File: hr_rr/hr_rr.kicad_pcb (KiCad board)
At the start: 2 copper layers, 5 parts, among them J1 Conn_01x02_Male, U1 TPS62746, U2 TPS63051_YFF, U3 nRF52840, U4 ADAS1000-4BCPZ

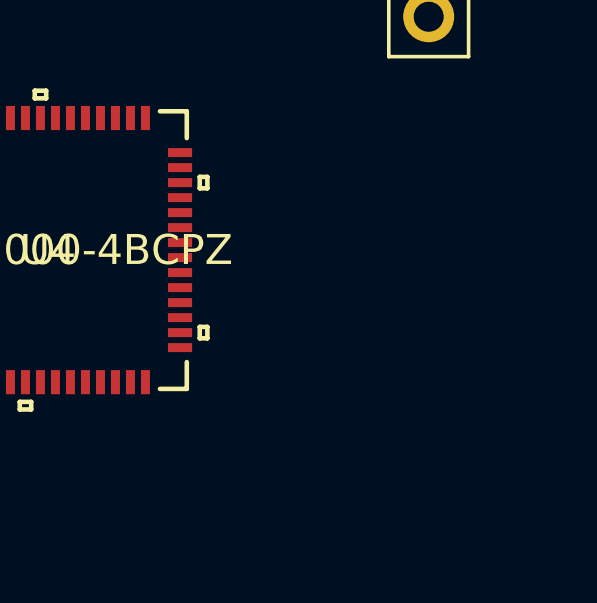
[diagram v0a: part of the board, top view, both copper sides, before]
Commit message: Restored original nRF52832 design.
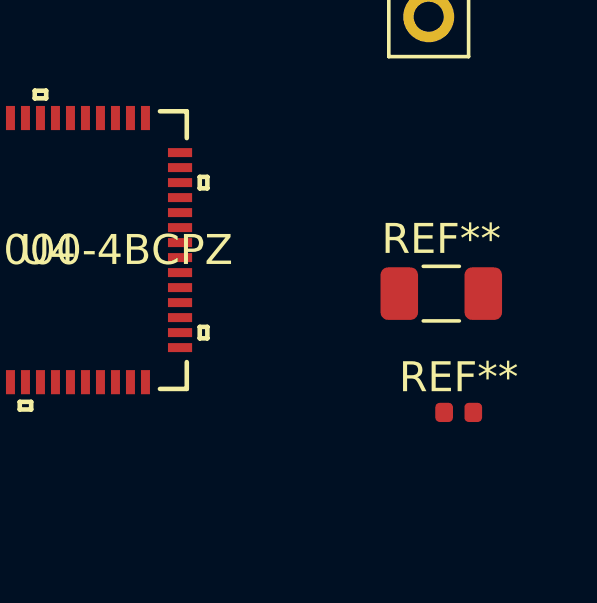
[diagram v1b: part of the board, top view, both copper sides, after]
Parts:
- added REF**: R_0402_1005Metric, Resistor_SMD:R_0402_1005Metric, F.Cu at (108.0, 72.3)
- added REF**: R_1206_3216Metric, Resistor_SMD:R_1206_3216Metric, F.Cu at (107.5, 68.4)
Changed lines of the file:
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@@
     (tracks 0)
     (zones 0)
-    (modules 5)
+    (modules 7)
     (nets 148)
   )
@@
     (pad_to_mask_clearance 0.2)
     (aux_axis_origin 0 0)
-    (visible_elements FFFFFF7F)
+    (visible_elements 7FFFFFFF)
     (pcbplotparams
       (layerselection 0x010fc_ffffffff)
@@
       (net 147 "Net-(U4-Pad56)"))
   )
+  (module Resistor_SMD:R_0402_1005Metric (layer F.Cu)
+    (at 108.04 72.34)
+    (descr "Resistor SMD 0402 (1005 Metric), square (rectangular) end terminal, IPC_7351 nominal, (Body size source: http://www.tortai-tech.com/upload/download/2011102023233369053.pdf), generated with kicad-footprint-generator")
+    (tags resistor)
+    (attr smd)
+    (fp_text reference REF** (at 0 -1.17) (layer F.SilkS)
+      (effects (font (size 1 1) (thickness 0.15)))
+    )
+    (fp_text value R_0402_1005Metric (at 0 1.17) (layer F.Fab)
+      (effects (font (size 1 1) (thickness 0.15)))
+    )
+    (fp_text user %R (at 0 0) (layer F.Fab)
+      (effects (font (size 0.25 0.25) (thickness 0.04)))
+    )
+    (fp_line (start 0.93 0.47) (end -0.93 0.47) (layer F.CrtYd) (width 0.05))
+    (fp_line (start 0.93 -0.47) (end 0.93 0.47) (layer F.CrtYd) (width 0.05))
+    (fp_line (start -0.93 -0.47) (end 0.93 -0.47) (layer F.CrtYd) (width 0.05))
+    (fp_line (start -0.93 0.47) (end -0.93 -0.47) (layer F.CrtYd) (width 0.05))
+    (fp_line (start 0.5 0.25) (end -0.5 0.25) (layer F.Fab) (width 0.1))
+    (fp_line (start 0.5 -0.25) (end 0.5 0.25) (layer F.Fab) (width 0.1))
+    (fp_line (start -0.5 -0.25) (end 0.5 -0.25) (layer F.Fab) (width 0.1))
+    (fp_line (start -0.5 0.25) (end -0.5 -0.25) (layer F.Fab) (width 0.1))
+    (pad 2 smd roundrect (at 0.485 0) (size 0.59 0.64) (layers F.Cu F.Paste F.Mask) (roundrect_rratio 0.25))
+    (pad 1 smd roundrect (at -0.485 0) (size 0.59 0.64) (layers F.Cu F.Paste F.Mask) (roundrect_rratio 0.25))
+    (model ${KISYS3DMOD}/Resistor_SMD.3dshapes/R_0402_1005Metric.wrl
+      (at (xyz 0 0 0))
+      (scale (xyz 1 1 1))
+      (rotate (xyz 0 0 0))
+    )
+  )
+  (module Resistor_SMD:R_1206_3216Metric (layer F.Cu)
+    (at 107.46 68.38)
+    (descr "Resistor SMD 1206 (3216 Metric), square (rectangular) end terminal, IPC_7351 nominal, (Body size source: http://www.tortai-tech.com/upload/download/2011102023233369053.pdf), generated with kicad-footprint-generator")
+    (tags resistor)
+    (attr smd)
+    (fp_text reference REF** (at 0 -1.82) (layer F.SilkS)
+      (effects (font (size 1 1) (thickness 0.15)))
+    )
+    (fp_text value R_1206_3216Metric (at 0 1.82) (layer F.Fab)
+      (effects (font (size 1 1) (thickness 0.15)))
+    )
+    (fp_text user %R (at 0 0) (layer F.Fab)
+      (effects (font (size 0.8 0.8) (thickness 0.12)))
+    )
+    (fp_line (start 2.28 1.12) (end -2.28 1.12) (layer F.CrtYd) (width 0.05))
+    (fp_line (start 2.28 -1.12) (end 2.28 1.12) (layer F.CrtYd) (width 0.05))
+    (fp_line (start -2.28 -1.12) (end 2.28 -1.12) (layer F.CrtYd) (width 0.05))
+    (fp_line (start -2.28 1.12) (end -2.28 -1.12) (layer F.CrtYd) (width 0.05))
+    (fp_line (start -0.602064 0.91) (end 0.602064 0.91) (layer F.SilkS) (width 0.12))
+    (fp_line (start -0.602064 -0.91) (end 0.602064 -0.91) (layer F.SilkS) (width 0.12))
+    (fp_line (start 1.6 0.8) (end -1.6 0.8) (layer F.Fab) (width 0.1))
+    (fp_line (start 1.6 -0.8) (end 1.6 0.8) (layer F.Fab) (width 0.1))
+    (fp_line (start -1.6 -0.8) (end 1.6 -0.8) (layer F.Fab) (width 0.1))
+    (fp_line (start -1.6 0.8) (end -1.6 -0.8) (layer F.Fab) (width 0.1))
+    (pad 2 smd roundrect (at 1.4 0) (size 1.25 1.75) (layers F.Cu F.Paste F.Mask) (roundrect_rratio 0.2))
+    (pad 1 smd roundrect (at -1.4 0) (size 1.25 1.75) (layers F.Cu F.Paste F.Mask) (roundrect_rratio 0.2))
+    (model ${KISYS3DMOD}/Resistor_SMD.3dshapes/R_1206_3216Metric.wrl
+      (at (xyz 0 0 0))
+      (scale (xyz 1 1 1))
+      (rotate (xyz 0 0 0))
+    )
+  )
 )

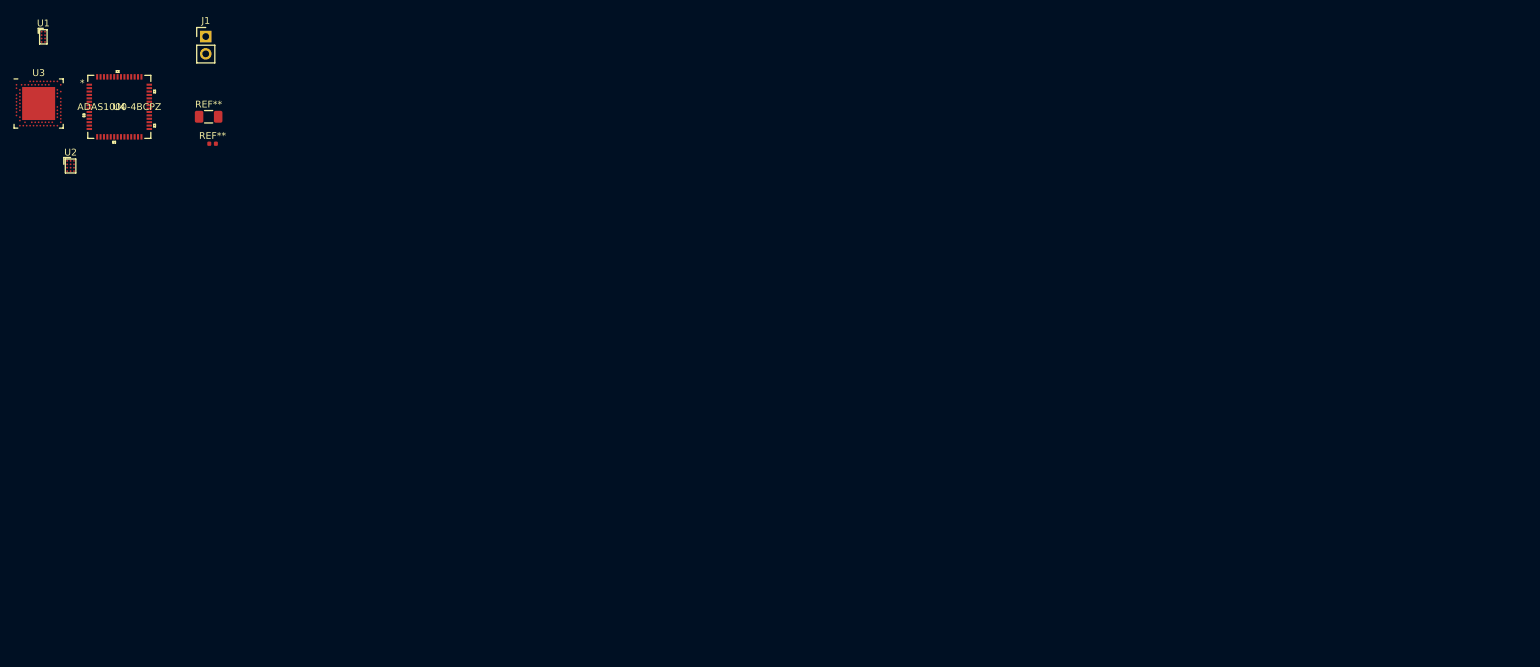
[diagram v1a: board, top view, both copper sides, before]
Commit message: Restored old PCB, reassigned new one. Removed unneeded components.
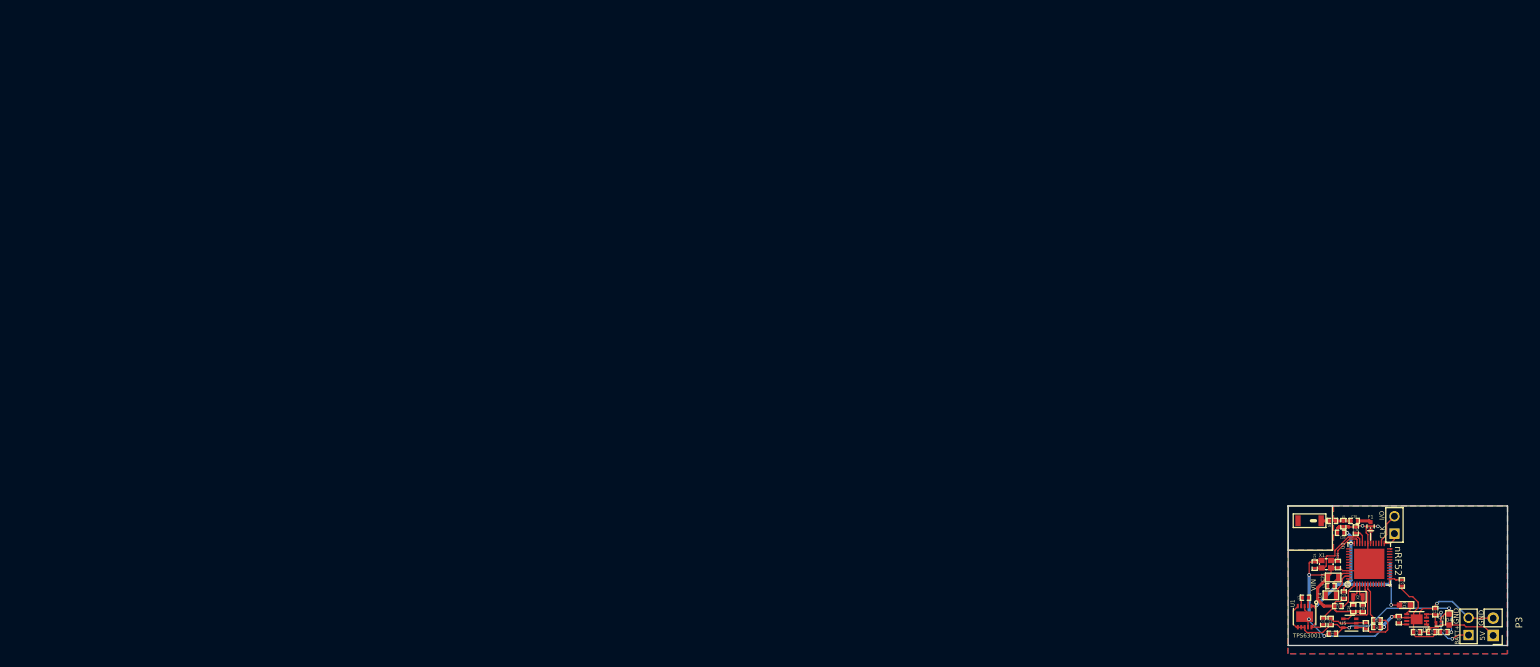
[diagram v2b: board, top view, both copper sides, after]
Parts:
- removed J1: Conn_01x02_Male, Connector_PinHeader_2.54mm:PinHeader_1x02_P2.54mm_Vertical
- removed REF**: R_0402_1005Metric, Resistor_SMD:R_0402_1005Metric
- removed REF**: R_1206_3216Metric, Resistor_SMD:R_1206_3216Metric
- removed U2: TPS63051_YFF, Package_BGA:Texas_DSBGA-12_1.36x1.86mm_Layout3x4_P0.5mm
- removed U4: ADAS1000-4BCPZ, footprints:ADAS1000-4BCPZ
- added A1: CHIP-ANT, JTI-2450AT18A100-CHIP-ANT, F.Cu at (269.0, 127.7)
- added C1: 10uF, SM0402, F.Cu at (272.1, 142.5)
- added C14: 10uF, SM0402, F.Cu at (277.3, 143.1)
- added C15: 10uF, SM0402, F.Cu at (272.4, 144.3)
- added C16: 4.7uF, SM0402, F.Cu at (284.8, 144.0)
- added C17: 4.7uF, SM0402, F.Cu at (287.5, 141.0)
- added C18: 1.0uF, SM0402, F.Cu at (288.8, 144.0)
- added C2: 22uF, SM0402, F.Cu at (271.0, 142.4)
- added C21: 4.7µF, SM0402, F.Cu at (274.1, 138.6)
- added C22: 100nF, SM0402, F.Cu at (282.6, 136.8)
- added C23: 1.0µF, SM0603, F.Cu at (272.5, 136.0)
- added C24: 12pF, SM0402, F.Cu at (269.8, 134.2)
- added C25: 12pF, SM0402, F.Cu at (273.2, 134.1)
- added C26: 100nF, SM0402, F.Cu at (273.2, 140.2)
- added C28: 12pF, SM0402, F.Cu at (275.4, 140.6)
- added C29: 12pF, SM0402, F.Cu at (276.9, 140.6)
- added C30: 1.0pF, SM0402, F.Cu at (275.6, 127.7)
- added C33: 100nF, SM0402, F.Cu at (273.6, 129.4)
- added C34: 100pF, SM0402, F.Cu at (275.8, 129.0)
- added D3: LED, LEDs:LED_0603, F.Cu at (283.0, 140.1)
- added D4: D_Schottky, LEDs:LED_0603, F.Cu at (289.5, 142.2)
- added F1: 2450FM07A0029, Resistors_SMD:R_0402, F.Cu at (278.0, 128.5)
- added L1: 2.20µH, SM0402, F.Cu at (268.4, 139.0)
- added L3: 15nH, SM0402, F.Cu at (272.2, 137.3)
- added L4: 10uH, SM0603, F.Cu at (272.2, 138.6)
- added L5: 2.7nH, SM0402, F.Cu at (274.0, 128.1)
- added L6: 3.9nH, SM0402, F.Cu at (272.4, 127.7)
- added P1: CONN_2, PIN_ARRAY_2X1, F.Cu at (292.4, 143.2)
- added P2: CONN_2, PIN_ARRAY_2X1, F.Cu at (281.5, 128.3)
- added P3: CONN_2, Pin_Headers:Pin_Header_Straight_1x02_Pitch2.54mm, F.Cu at (296.0, 144.5)
- added Q1: DMP21D5UFB4-7B, pwr_pads:X2-DFN1006, F.Cu at (288.0, 142.7)
- added R10: 100k, SM0402, F.Cu at (287.0, 144.0)
- added R5: 1M, SM0402, F.Cu at (278.9, 142.3)
- added R7: 1M, SM0402, F.Cu at (278.9, 143.3)
- added R9: 2k, SM0402, F.Cu at (282.1, 142.2)
- added U5: TPS2294x, TO_SOT_Packages_SMD:SOT-353_SC-70-5, F.Cu at (274.9, 142.7)
- added U6: MCP73831, Housings_DFN_QFN:DFN-8-1EP_3x2mm_Pitch0.5mm, F.Cu at (284.8, 142.1)
- added X1: Crystal_GND24, CRYSTAL-SMD-2.0MMx1.6MM, F.Cu at (271.5, 134.1)
- added X2: 32.768 kHz, Crystals:Crystal_SMD_2012-2pin_2.0x1.2mm, F.Cu at (276.1, 138.8)
- U1: value TPS62746 -> TPS63001; footprint Package_BGA:Texas_DSBGA-8_0.9x1.9mm_Layout2x4_P0.5mm -> Housings_DFN_QFN:DFN-10-1EP_3x3mm_Pitch0.5mm
- U3: value nRF52840 -> NRF528XX-QFAA; footprint Package_DFN_QFN:Nordic_AQFN-73-1EP_7x7mm_P0.5mm -> Housings_DFN_QFN:UQFN-48-1EP_6x6mm_Pitch0.4mm
- moved U3 206.6 mm to (277.8, 134.0), turned to 90 degrees
- moved U1 203.7 mm to (268.3, 141.8), turned to 270 degrees
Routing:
- net DGND: track 0.00 -> 123.7 mm, vias 0 -> 8
- net DVDD: track 0.00 -> 40.4 mm, vias 0 -> 6
- net VCC: track 0.00 -> 37.3 mm, vias 0 -> 3
- net 5V_in_charge: track 0.00 -> 13.8 mm
- net /BATT_IN: track 0.00 -> 11.5 mm, vias 0 -> 2
- net Net-(C24-Pad2): track 0.00 -> 11.0 mm
- net /LOAD_SW_CTRL: track 0.00 -> 8.38 mm
- net Net-(C14-Pad1): track 0.00 -> 7.34 mm
- net Net-(C25-Pad2): track 0.00 -> 6.76 mm
- net /AIN_BAT_DIV_VOLTAGE: track 0.00 -> 6.63 mm
- net /SWDIO: track 0.00 -> 4.77 mm
- net /DEC1: track 0.00 -> 4.32 mm
- net Net-(L4-Pad1): track 0.00 -> 3.92 mm
- net Net-(C28-Pad1): track 0.00 -> 3.33 mm
- net Net-(C23-Pad1): track 0.00 -> 3.32 mm
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- added copper zone on B.Cu, net DGND
- added copper zone on F.Cu, net DGND
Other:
- board outline added: 32.2 x 20.5 mm
- net class Default: clearance 0.2 -> 0.1524; trace_width 0.25 -> 0.4572; via_dia 0.8 -> 0.508; via_drill 0.4 -> 0.3302
- rule pad_to_mask_clearance: 0.2 -> 0.015
- rule trace_clearance: 0.2 -> 0.1524
- rule trace_min: 0.2 -> 0.05
- rule via_min_drill: 0.3 -> 0.3302
- rule via_min_size: 0.4 -> 0.152
- board text added: "5V"
- board text added: "BATT+"
- board text added: "CLK"
- board text added: "GND"
- board text added: "I/O"
- board text added: "TPS63001"
- board text added: "Todo, separate DGND and AVSS"
- board text added: "VIN"
- board text added: "nRF52"
- board text added: "nRF52-GSR Prototype 09/03/18 Yeo GaTech BNE Lab"

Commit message: Cleaned PCB of old voltage regulators.
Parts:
- removed U1: TPS63001, Housings_DFN_QFN:DFN-10-1EP_3x3mm_Pitch0.5mm
- removed U5: TPS2294x, TO_SOT_Packages_SMD:SOT-353_SC-70-5
- L1: value 2.20µH -> L_0603_1608Metric; footprint SM0402 -> Inductor_SMD:L_0603_1608Metric
- moved L1 1.83 mm to (268.7, 140.8)
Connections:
- L1 pad 1: Net-(L1-Pad1) -> (no net)
- L1 pad 2: Net-(L1-Pad2) -> (no net)
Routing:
- net DGND: track 123.7 -> 85.0 mm, vias 8 -> 4
- net VCC: track 37.3 -> 7.20 mm, vias 3 -> 2
- net DVDD: track 40.4 -> 29.6 mm, vias 6 -> 5
- net /LOAD_SW_CTRL: track 8.38 -> 6.85 mm
- net Net-(L1-Pad1): track 1.30 -> 0.00 mm
- net Net-(L1-Pad2): track 1.26 -> 0.00 mm
- net Net-(C14-Pad1): track 7.34 -> 6.12 mm
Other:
- board text removed: "TPS63001"

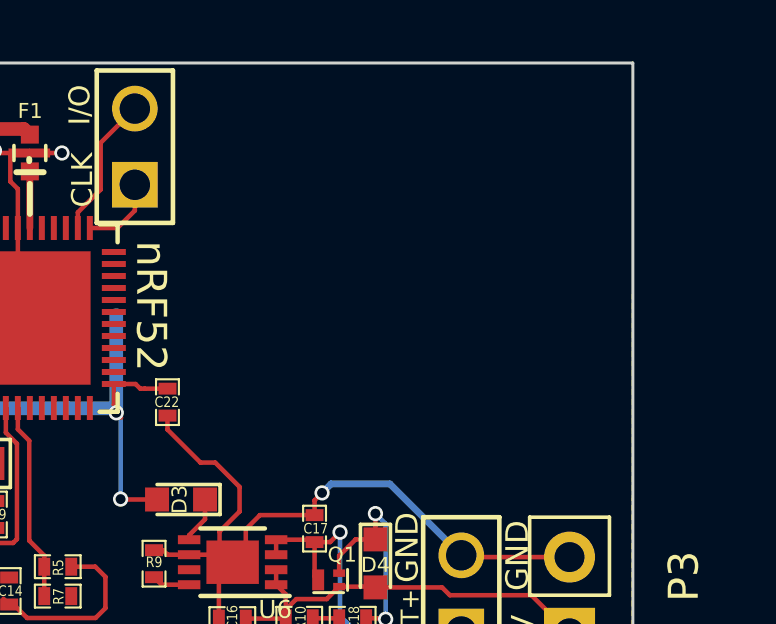
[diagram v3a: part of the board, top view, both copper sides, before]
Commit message: Updated footprint to include new footprints.
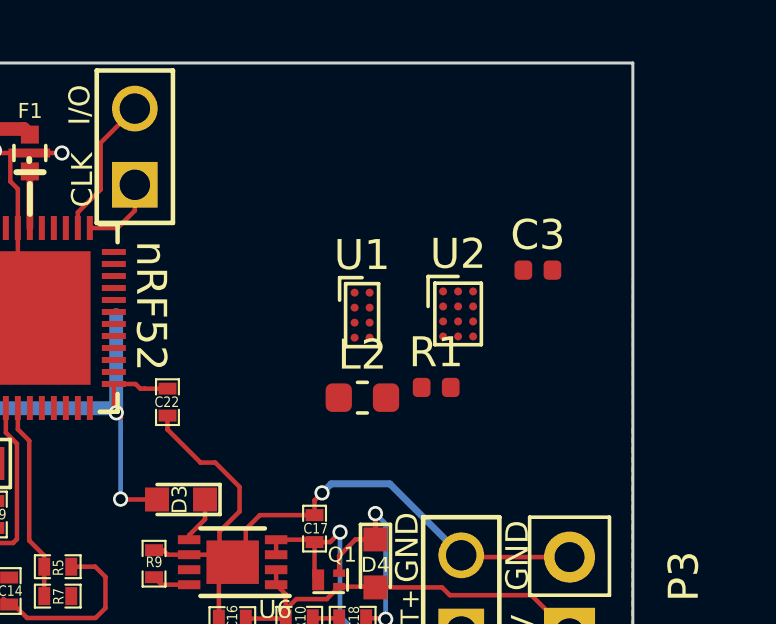
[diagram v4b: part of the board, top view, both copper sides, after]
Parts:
- added C3: 1nF, Capacitor_SMD:C_0402_1005Metric, F.Cu at (294.9, 132.4)
- added L2: 2.20 µH, Inductor_SMD:L_0603_1608Metric, F.Cu at (289.1, 136.7)
- added R1: 1M, Resistor_SMD:R_0402_1005Metric, F.Cu at (291.5, 136.3)
- added U1: TPS62746, Package_BGA:Texas_DSBGA-8_0.9x1.9mm_Layout2x4_P0.5mm, F.Cu at (289.1, 133.9)
- added U2: TPS63051_YFF, Package_BGA:Texas_DSBGA-12_1.36x1.86mm_Layout3x4_P0.5mm, F.Cu at (292.3, 133.9)
- C1: value 10uF -> 10µF
- C2: value 22uF -> 22µF
- L1: value L_0603_1608Metric -> 2.20 µH
- L5: value 2.7nH -> 2.7 nH
- L6: value 3.9nH -> 3.9 nH
- P1, P2, P3: value CONN_2 -> Conn_01x02_Male
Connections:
- net /ALERT renamed Net-(U3-Pad22)
- net /SCL renamed Net-(U3-Pad23)
- net /SDA renamed Net-(U3-Pad24)
- net VCC renamed Vcc<BATT>
- C14 pad 1: Net-(C14-Pad1) -> 1.8V_supply
- C2 pad 1: DVDD -> 3.3V_supply
- C21 pad 2: DVDD -> 1.8V_supply
- C22 pad 1: DVDD -> 1.8V_supply
- C33 pad 2: DVDD -> 1.8V_supply
- D3 pad 2: DVDD -> 1.8V_supply
- L1 pad 1: (no net) -> Net-(L1-Pad1)
- L1 pad 2: (no net) -> Net-(L1-Pad2)
- P1 pad 1: /BATT_IN -> BATT_V
- Q1 pad 2: /BATT_IN -> BATT_V
- R5 pad 1: /AIN_BAT_DIV_VOLTAGE -> Net-(R5-Pad1)
- R5 pad 2: Net-(C14-Pad1) -> /AIN_BAT_DIV_VOLTAGE
- U3 pad 13: DVDD -> 1.8V_supply
- U3 pad 36: DVDD -> 1.8V_supply
- U3 pad 48: DVDD -> 1.8V_supply
- U3 pad 7: /GSR_AIN -> /PG_TPS63051
- U3 pad 8: Net-(U3-Pad8) -> /ILIM0_TPS63051
- U3 pad 9: Net-(U3-Pad9) -> /ILIM1_TPS63051
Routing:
- net DVDD: track 29.6 -> 0.00 mm, vias 5 -> 0
- net 1.8V_supply: track 0.00 -> 29.6 mm, vias 0 -> 5
